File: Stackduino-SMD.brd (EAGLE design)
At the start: 62.5 x 68 mm, 60 parts

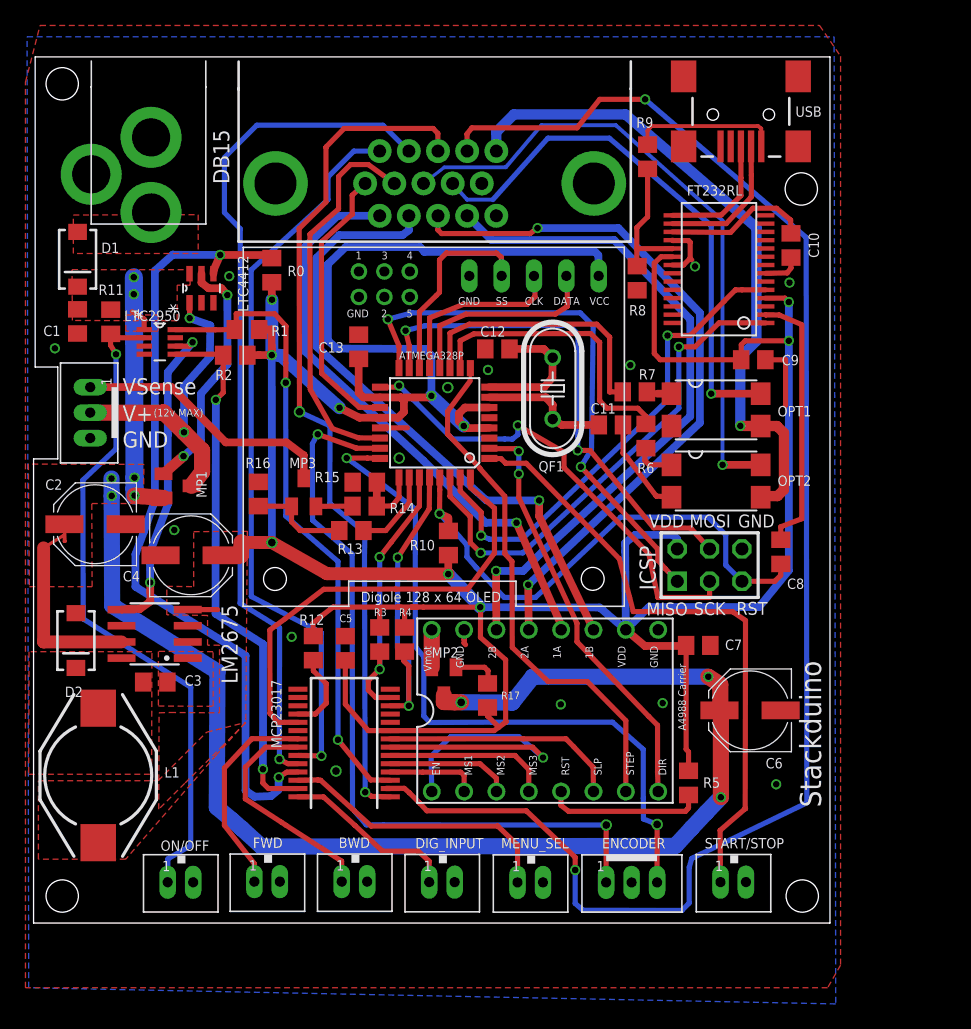
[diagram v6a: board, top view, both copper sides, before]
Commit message: added camera input
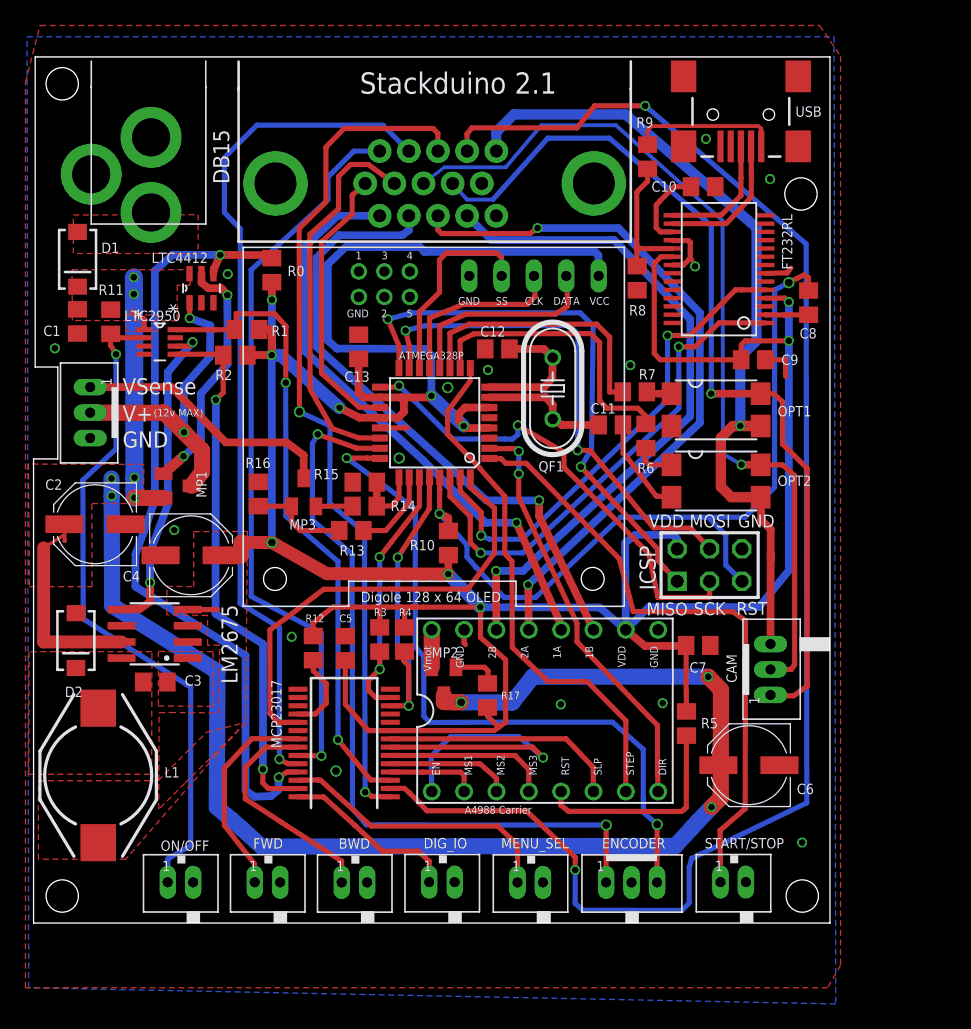
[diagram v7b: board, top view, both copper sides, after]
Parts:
- added CAM: JST-PH_3-PIN_HEADER, SRG:JST_B3B-PH_HEADER
- moved C8 19.7 mm to (60.0, 60.2), turned to 270 degrees
- moved C10 8.30 mm to (51.7, 69.3), turned to 0 degrees
- moved R5 4.66 mm to (50.4, 27.1)
- moved C6 4.31 mm to (55.3, 23.8)
- moved BWD 0.06 mm to (24.4, 14.7)
- moved FWD 0.06 mm to (17.6, 14.7)
- renumbered DIG_INPUT to DIG_IO
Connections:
- net CAM_GND: now also CAM.P3
- net OPT1: now also CAM.P2
- net OPT2: now also CAM.P1
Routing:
- net OPT2: track 42.7 -> 70.9 mm
- net N$11: track 42.9 -> 63.5 mm, vias 1 -> 2
- net OPT1: track 50.5 -> 69.7 mm
- net N$3: track 21.0 -> 3.39 mm
- net CAM_GND: track 52.1 -> 66.9 mm
- net V+: track 145.1 -> 152.2 mm
- net N$43: track 11.5 -> 6.54 mm
- net VCC: track 272.3 -> 267.5 mm
- net N$2: track 12.4 -> 16.8 mm
- net GND: track 23.6 -> 20.5 mm, vias 14 -> 15
- net DIG2: track 121.7 -> 120.9 mm
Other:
- board text added: "Stackduino 2.1"
- board text removed: "Stackduino"

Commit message: Beginning to re-layout traces on grid
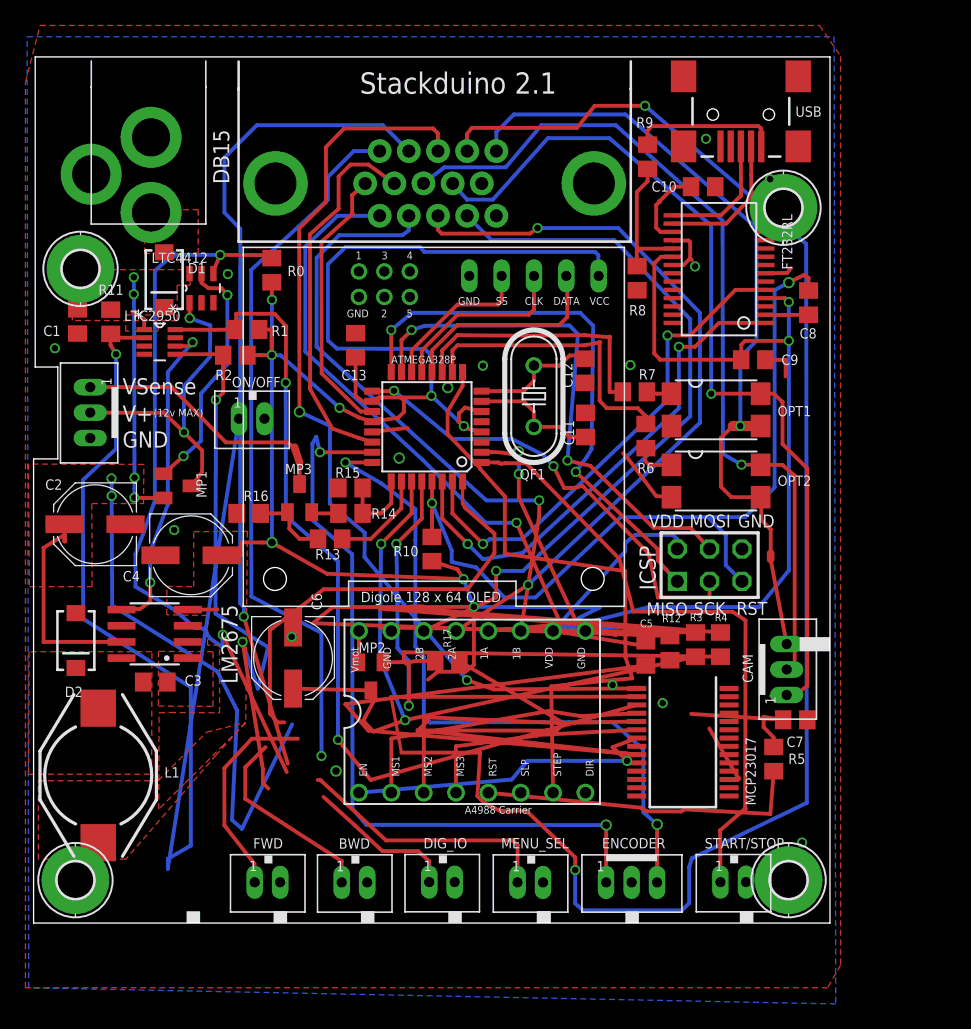
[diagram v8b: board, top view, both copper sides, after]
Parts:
- added H1, H2, H3, H4: MOUNT-PAD-ROUND2.8, holes:2,8-PAD
- moved ON/OFF 36.8 mm to (16.3, 51.1)
- moved C6 36.8 mm to (19.5, 32.2), turned to 270 degrees
- moved R12 28.0 mm to (49.1, 33.0)
- moved MCP23017 26.6 mm to (50.1, 25.6), turned to 270 degrees
- moved R4 24.8 mm to (53.0, 33.3)
- moved R3 24.8 mm to (51.1, 33.3)
- moved C5 23.6 mm to (47.2, 32.6)
- moved C7 9.60 mm to (58.9, 27.4)
- moved R5 7.41 mm to (57.2, 24.3)
- moved C12 7.08 mm to (42.4, 54.8), turned to 270 degrees
- moved D1 6.99 mm to (9.37, 62.0)
- moved MP2 5.74 mm to (25.6, 30.8)
- moved A4988_CARRIER 5.71 mm to (25.9, 33.1)
- moved R17 4.16 mm to (31.6, 32.0), turned to 0 degrees
- moved C11 2.00 mm to (42.5, 50.5), turned to 90 degrees
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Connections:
- net GND: now also H1.B2,8, H2.B2,8, H3.B2,8, H4.B2,8
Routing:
- net VCC: track 267.5 -> 457.0 mm
- net V+: track 152.2 -> 86.9 mm, vias 9 -> 6
- net PBUTTON: track 52.7 -> 87.4 mm
- net N$19: track 21.6 -> 49.4 mm
- net DIG2: track 120.9 -> 146.4 mm
- net N$18: track 25.0 -> 48.1 mm
- net KILL: track 50.2 -> 70.4 mm
- net SLEEP: track 18.8 -> 0.00 mm
- net MS1: track 7.18 -> 23.7 mm
- net MS2: track 9.81 -> 22.7 mm
- net N$2: track 16.8 -> 25.7 mm
- net STEP: track 41.3 -> 49.1 mm
- net DIR: track 32.7 -> 25.4 mm
- net N$8: track 6.37 -> 0.00 mm
- net INT: track 42.6 -> 48.3 mm
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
